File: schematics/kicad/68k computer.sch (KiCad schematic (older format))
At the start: 1 part, among them U3 68000D

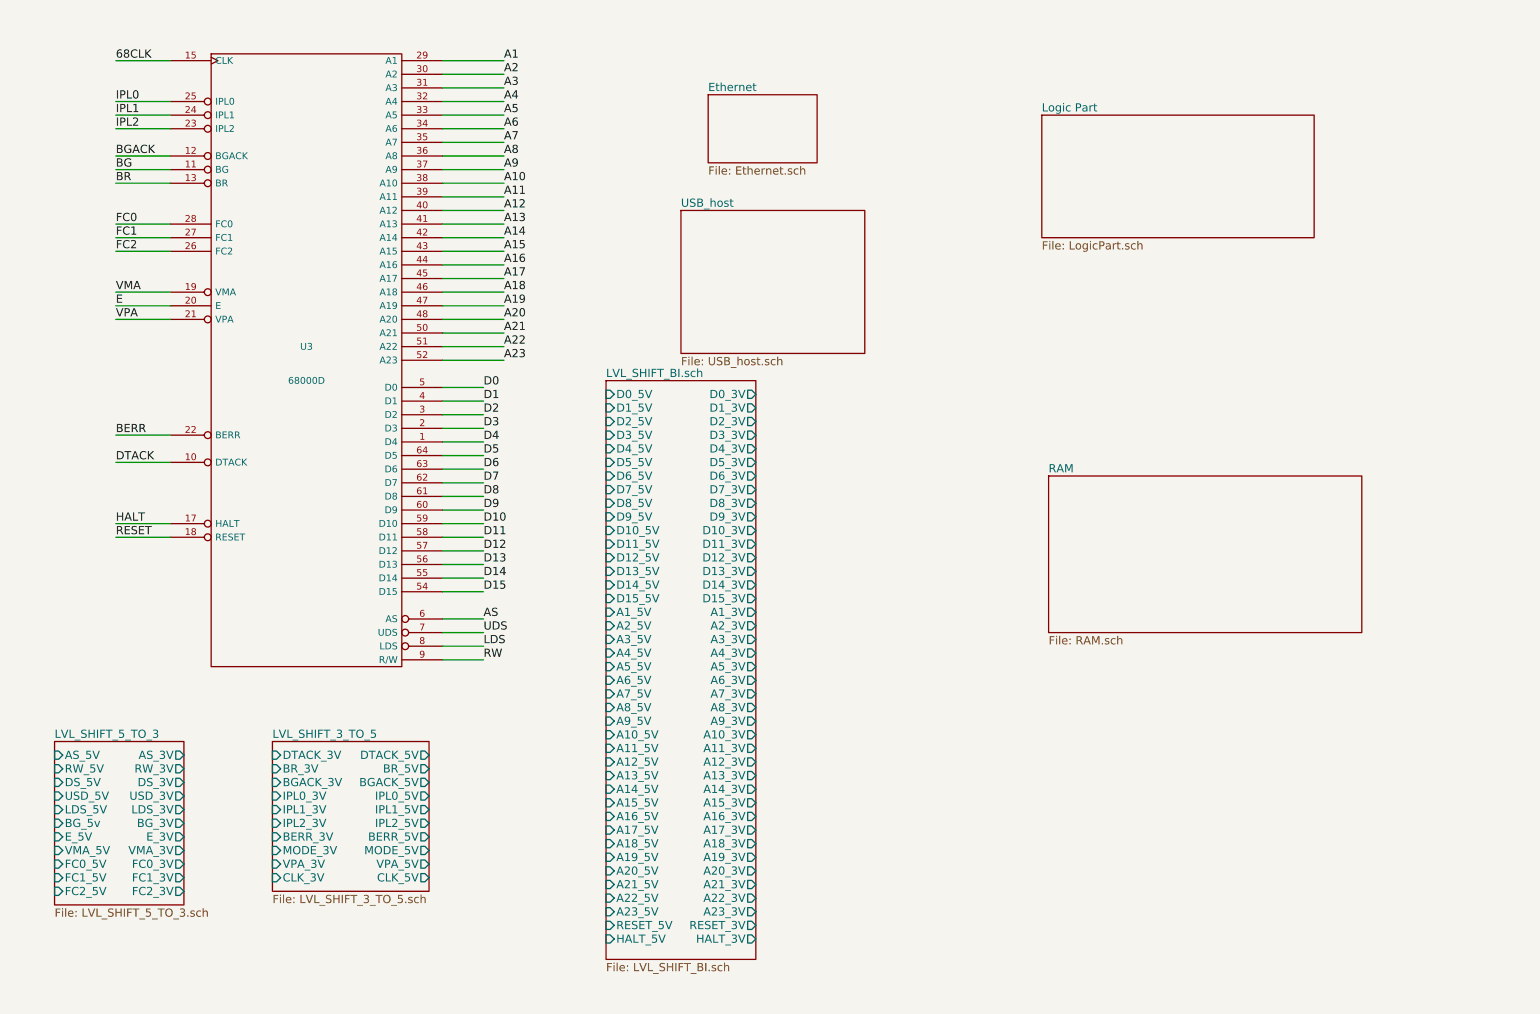
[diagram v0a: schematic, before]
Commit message: Add many hierarchical pins
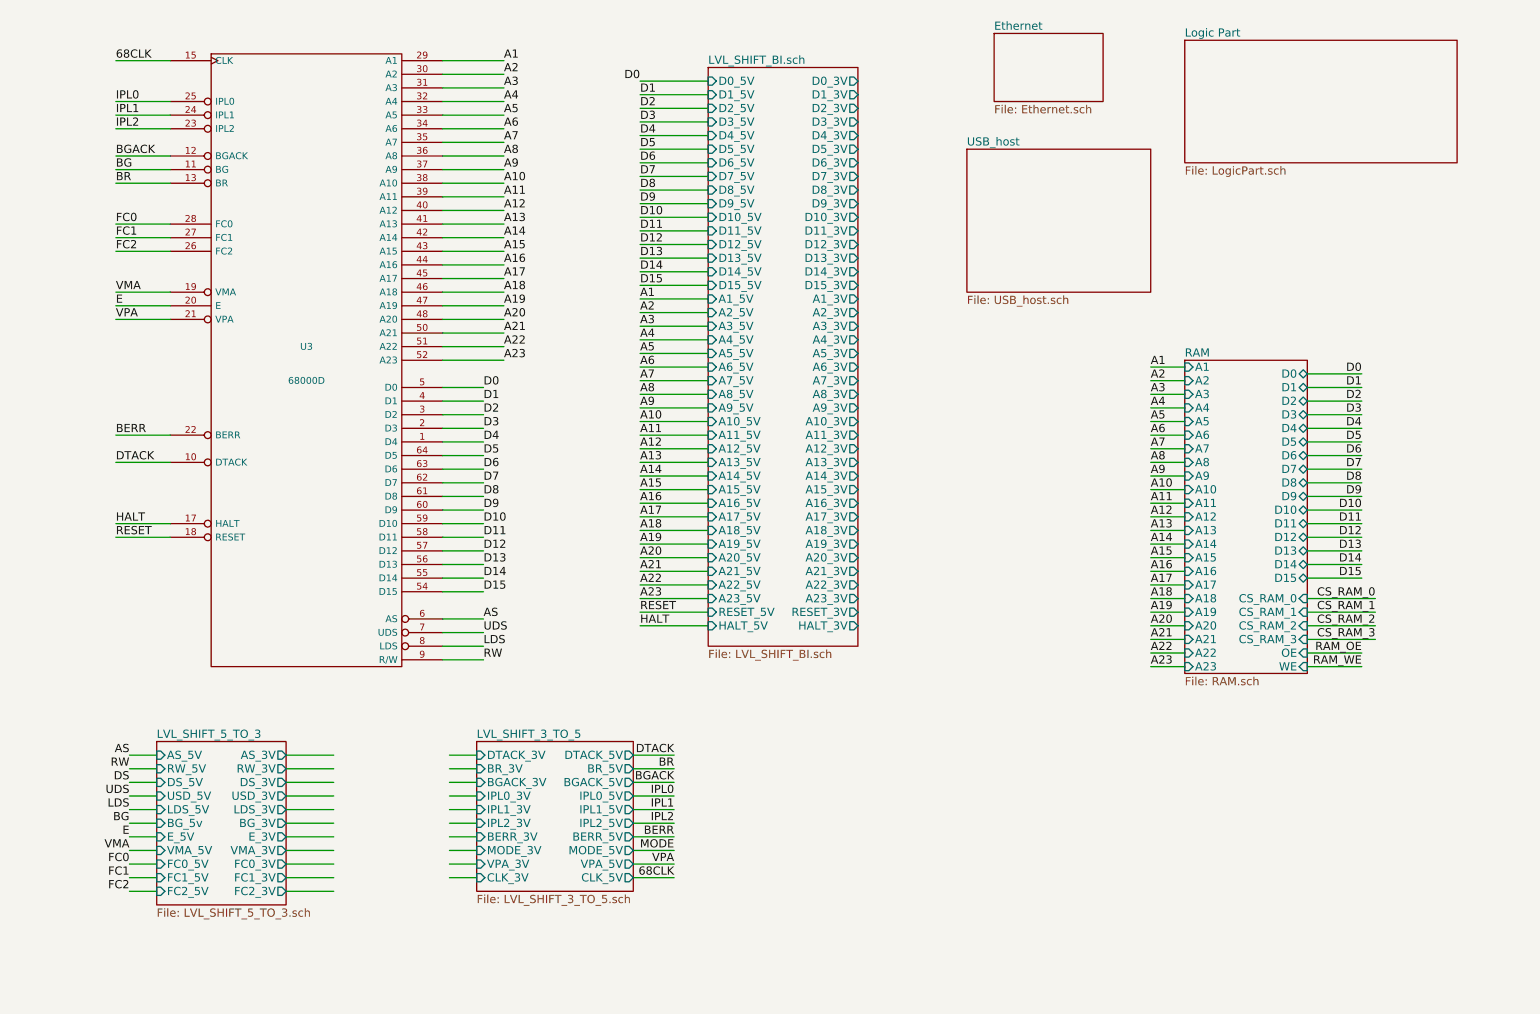
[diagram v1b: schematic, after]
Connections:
- net labels added: CS_RAM_0, CS_RAM_1, CS_RAM_2, CS_RAM_3, DS, MODE, RAM_OE, RAM_WE
- wire segments 60 -> 188

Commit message: Change a lot of things, especially pinning between sheets
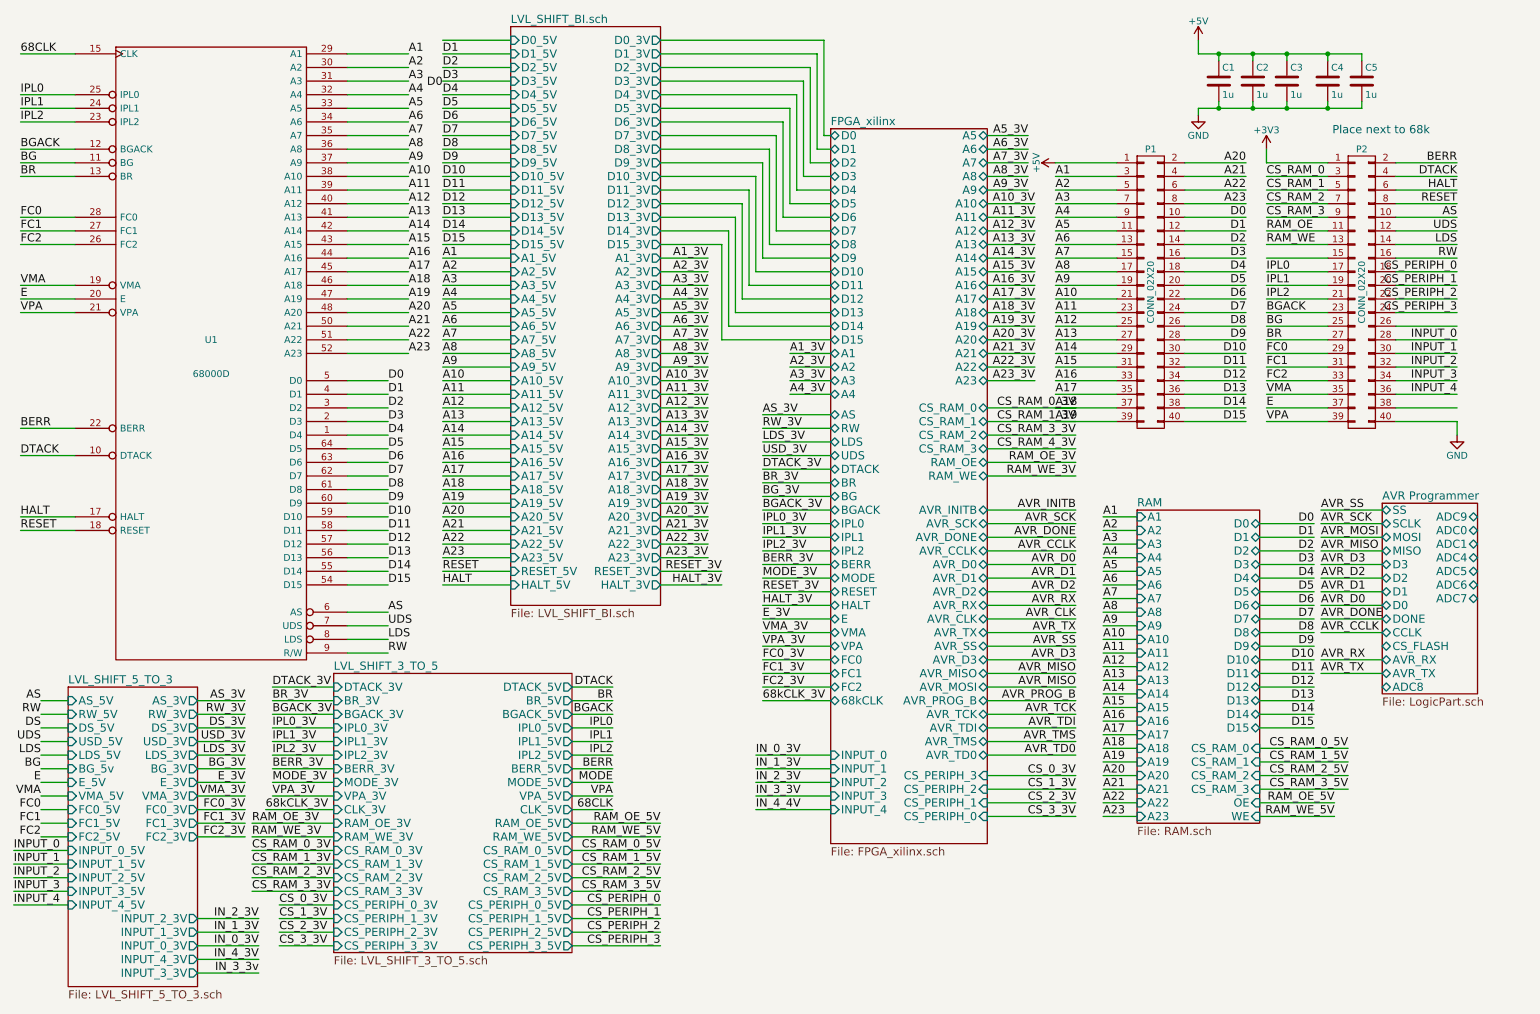
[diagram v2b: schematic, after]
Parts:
- added C1, C2, C3, C4, C5: 1u, symbol C
- added P1, P2: CONN_02X20, symbol CONN_02X20
- renumbered U3 to U1
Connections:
- net labels added: +3V3, +5V, 68kCLK_3V, A10_3V, A11_3V, A12_3V, A13_3V, A14_3V, A15_3V, A16_3V, A17_3V, A18_3V, A19_3V, A1_3V, A20_3V, A21_3V, A22_3V, A23_3V, A2_3V, A3_3V, A4_3V, A5_3V, A6_3V, A7_3V, A8_3V, A9_3V, AS_3V, AVR_CCLK, AVR_CLK, AVR_D0, AVR_D1, AVR_D2, AVR_D3, AVR_DONE, AVR_INITB, AVR_MISO, AVR_MOSI, AVR_PROG_B, AVR_RX, AVR_SCK, AVR_SS, AVR_TCK, AVR_TD0, AVR_TDI, AVR_TMS, AVR_TX, BERR_3V, BGACK_3V, BG_3V, BR_3V, CS_0_3V, CS_1_3V, CS_2_3V, CS_3_3V, CS_PERIPH_0, CS_PERIPH_1, CS_PERIPH_2, CS_PERIPH_3, CS_RAM_0_3V, CS_RAM_0_5V, CS_RAM_1_3V, CS_RAM_1_5V, CS_RAM_2_3V, CS_RAM_2_5V, CS_RAM_3_3V, CS_RAM_3_5V, CS_RAM_4_3V, DS_3V, DTACK_3V, E_3V, FC0_3V, FC1_3V, FC2_3V, GND, HALT_3V, INPUT_0, INPUT_1, INPUT_2, INPUT_3, INPUT_4, IN_0_3V, IN_1_3V, IN_2_3V, IN_3_3V, IN_3_3v, IN_4_3V, IN_4_4V, IPL0_3V, IPL1_3V, IPL2_3V, LDS_3V, MODE_3V, RAM_OE_3V, RAM_OE_5V, RAM_WE_3V, RAM_WE_5V, RESET_3V, RW_3V, USD_3V, VMA_3V, VPA_3V
- wire segments 188 -> 478
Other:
- note added: "Place next to 68k\n"
- moved on the sheet: U1
